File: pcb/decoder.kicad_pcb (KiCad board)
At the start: 2 copper layers, 50 x 30 mm, 76 parts, among them J1 Conn_01x03_Socket, J2 Conn_01x03_Socket, J3 Conn_01x02_Socket, J4 Conn_01x02_Socket, J5 Conn_01x02_Socket, J6 Conn_01x02_Socket, J7 Conn_01x02_Socket, J8 Conn_01x03_Socket, Q1 IRLZ44N, Q10 BC817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

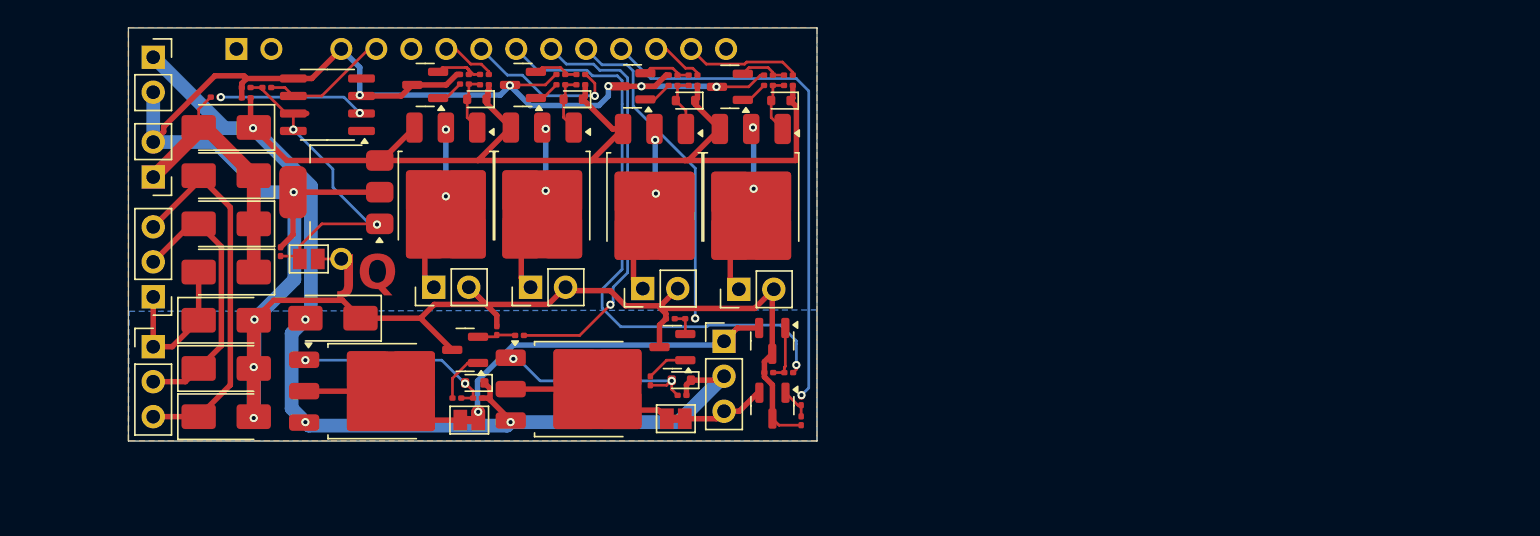
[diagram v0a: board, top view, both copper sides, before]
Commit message: make PCB smaller
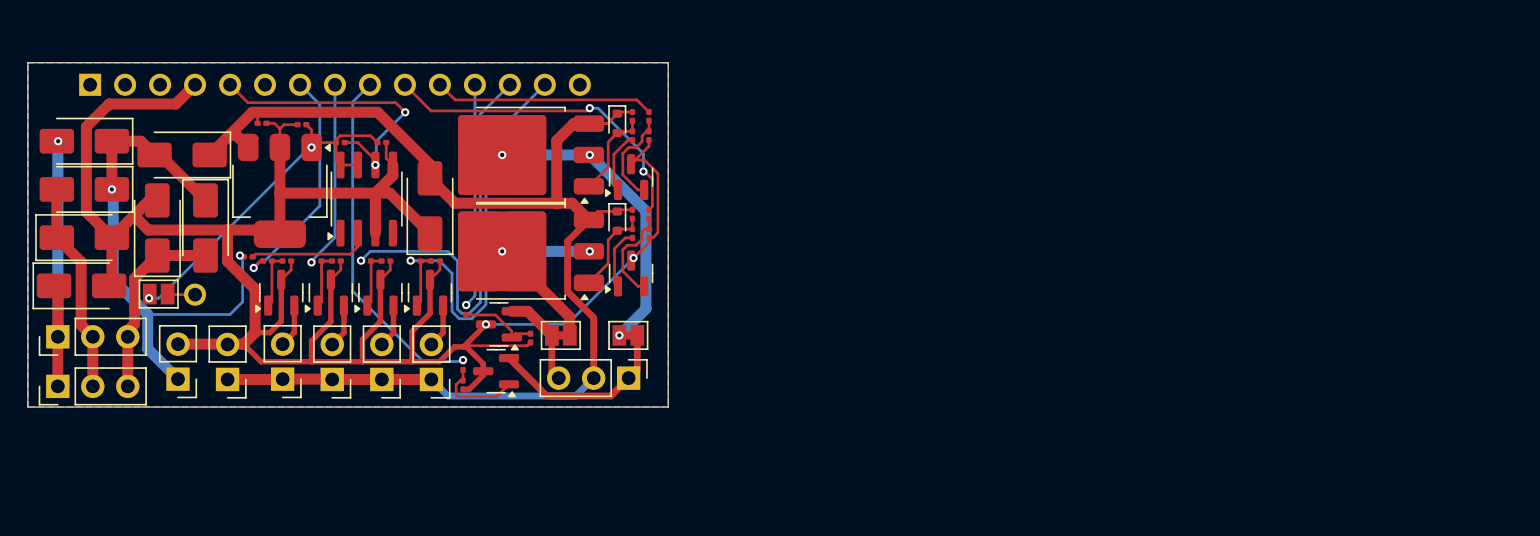
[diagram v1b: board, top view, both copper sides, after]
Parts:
- removed D10, D13, D14, D9: 15V, Diode_SMD:D_SOD-523
- removed J7: Conn_01x02_Socket, Connector_PinHeader_2.54mm:PinHeader_1x02_P2.54mm_Vertical
- removed Q11, Q13, Q9: FQP27P06, Package_TO_SOT_SMD:TO-252-3_TabPin2
- removed Q12, Q15: BC817, Package_TO_SOT_SMD:SOT-23
- removed R19, R28: 100, Capacitor_SMD:C_0201_0603Metric
- removed R20, R22, R26, R30: 2k, Capacitor_SMD:C_0201_0603Metric
- removed R21, R25, R27, R29: 100k, Capacitor_SMD:C_0201_0603Metric
- removed REF**: PinSocket_1x02_P2.54mm_Vertical, Connector_PinSocket_2.54mm:PinSocket_1x02_P2.54mm_Vertical
- added C1: 1mF, Connector_PinHeader_2.54mm:PinHeader_1x02_P2.54mm_Vertical, F.Cu at (39.1, 48.0)
- added J9: Conn_01x02_Socket, Connector_PinHeader_2.54mm:PinHeader_1x02_P2.54mm_Vertical, F.Cu at (50.3, 48.0)
- added Q14: FDN5630, Package_TO_SOT_SMD:SOT-23, F.Cu at (50.2, 41.7)
- added R31: 100k, Capacitor_SMD:C_0201_0603Metric, F.Cu at (50.6, 39.4)
- added R32: 100, Capacitor_SMD:C_0201_0603Metric, F.Cu at (49.2, 39.4)
- D11, D12: value 15V -> BZT52C15
- D8: value D_TVS -> SMBJ24CA
- Q1, Q4: value IRLZ44N -> FDN5630
- Q10, Q8: value BC817 -> FDN5630
- Q7: value FQP27P06 -> FDN5630; footprint Package_TO_SOT_SMD:TO-252-3_TabPin2 -> Package_TO_SOT_SMD:SOT-23
- R18: value 100k -> 100
- moved Q10 26.4 mm to (53.8, 41.7), turned to 90 degrees
- moved R18 26.1 mm to (42.0, 39.4), turned to 180 degrees
- moved R5 25.2 mm to (56.4, 43.0)
- moved R14 23.7 mm to (56.2, 47.0), turned to 90 degrees
- moved R4 23.3 mm to (68.5, 28.9), turned to -90 degrees
- moved R8 22.9 mm to (68.5, 30.3), turned to 90 degrees
- moved R23 22.6 mm to (54.2, 39.4), turned to 180 degrees
- moved R24 22.6 mm to (52.8, 39.4), turned to 180 degrees
- moved R6 22.2 mm to (56.2, 48.4), turned to 90 degrees
- moved D11 21.5 mm to (67.4, 29.4), turned to -90 degrees
- moved Q1 20.7 mm to (58.8, 44.0), turned to 180 degrees
- moved R2 20.5 mm to (61.1, 45.0)
- moved Q4 20.2 mm to (58.6, 47.4), turned to 180 degrees
- moved Q3 20.2 mm to (60.3, 31.7), turned to 180 degrees
- moved R17 18.7 mm to (43.4, 39.4)
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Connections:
- net 5V renamed /5V
- net AC1 renamed Net-(D15-A)
- net AC2 renamed Net-(D1-A)
- net AC3 renamed Net-(D2-A)
- net Motor_A renamed /Motor_A
- net Motor_A1 renamed /Motor_A1
- net Motor_B renamed /Motor_B
- net Motor_B1 renamed /Motor_B1
- net VCC renamed /VCC
- A1 pad 4: GND -> /GND
- C2 pad 2: GND -> /GND
- C4 pad 1: GND -> /GND
- C5 pad 1: GND -> /GND
- C5 pad 2: VM -> /VM
- D11 pad 1: VM -> /VM
- D12 pad 1: VM -> /VM
- D3 pad 2: GND -> /GND
- D4 pad 2: GND -> /GND
- D5 pad 2: GND -> /GND
- D6 pad 1: VM -> /VM
- D8 pad 1: GND -> /GND
- D8 pad 2: VM -> /VM
- J3 pad 2: GND -> /GND
- J4 pad 1: Lamp2 -> /VM
- J4 pad 2: GND -> Net-(J4-Pin_2)
- J5 pad 1: Lamp1 -> /VM
- J5 pad 2: GND -> Net-(J5-Pin_2)
- J6 pad 1: Lamp3 -> /VM
- J6 pad 2: GND -> Net-(J6-Pin_2)
- J8 pad 2: VM -> /VM
- Q1 pad 3: GND -> /GND
- Q10 pad 1: Net-(Q10-C) -> Net-(Q10-G)
- Q10 pad 2: Net-(Q10-B) -> Net-(J6-Pin_2)
- Q10 pad 3: GND -> /GND
- Q2 pad 3: VM -> /VM
- Q3 pad 3: VM -> /VM
- Q4 pad 3: GND -> /GND
- Q5 pad 3: GND -> /GND
- Q6 pad 3: GND -> /GND
- Q7 pad 1: Net-(D10-A) -> Net-(Q7-G)
- Q7 pad 2: Lamp2 -> Net-(J4-Pin_2)
- Q7 pad 3: VM -> /GND
- Q8 pad 1: Net-(Q8-C) -> Net-(Q8-G)
- Q8 pad 2: Net-(Q8-B) -> Net-(J5-Pin_2)
- Q8 pad 3: GND -> /GND
- R10 pad 2: GND -> /GND
- R11 pad 2: VM -> /VM
- R12 pad 1: Net-(A1-D7) -> Net-(A1-D8)
- R13 pad 2: GND -> /GND
- R15 pad 1: Net-(D9-A) -> /GND
- R15 pad 2: VM -> Net-(Q7-G)
- R16 pad 1: Net-(Q8-C) -> Net-(Q7-G)
- R16 pad 2: Net-(D9-A) -> Net-(A1-D5)
- R17 pad 1: Net-(Q8-B) -> /GND
- R17 pad 2: GND -> Net-(Q8-G)
- R18 pad 1: Net-(D10-A) -> Net-(Q8-G)
- R18 pad 2: VM -> Net-(A1-D4)
- R2 pad 1: GND -> /GND
- R23 pad 1: Net-(D13-A) -> /GND
- R23 pad 2: VM -> Net-(Q10-G)
- R24 pad 1: Net-(Q12-C) -> Net-(Q10-G)
- R24 pad 2: Net-(D13-A) -> Net-(A1-D11)
- R4 pad 1: VM -> /VM
- R6 pad 1: GND -> /GND
- R9 pad 1: Net-(A1-D8) -> Net-(A1-D7)
- U1 pad 2: GND -> /GND
- U1 pad 3: VM -> /VM
- U3 pad 3: GND -> /GND
- U3 pad 5: GND -> /GND
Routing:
- net GND: track 185.0 -> 0.00 mm, vias 9 -> 0
- net /GND: track 0.00 -> 166.1 mm, vias 0 -> 2
- net VM: track 148.4 -> 0.00 mm, vias 4 -> 0
- net /VM: track 0.00 -> 91.2 mm
- net Net-(A1-D10): track 3.88 -> 30.0 mm, vias 0 -> 1
- net Net-(A1-D9): track 37.2 -> 16.4 mm
- net /VCC: track 20.0 -> 38.9 mm, vias 0 -> 2
- net Net-(A1-D11): track 8.42 -> 27.1 mm, vias 0 -> 1
- net Net-(A1-D6): track 43.3 -> 25.8 mm
- net Net-(D15-A): track 27.8 -> 13.9 mm
- net Net-(A1-D4): track 3.97 -> 16.9 mm, vias 0 -> 1
- net /Motor_B1: track 9.90 -> 22.3 mm, vias 0 -> 3
- net Net-(A1-D2): track 9.30 -> 21.4 mm, vias 0 -> 2
- net /Motor_B: track 24.9 -> 13.7 mm, vias 1 -> 0
- net Net-(D2-A): track 11.2 -> 21.7 mm, vias 0 -> 1
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- added copper zone on B.Cu, net /GND
- added copper zone on F.Cu, net /VM
- removed copper zone on F.Cu, net GND
- removed copper zone on B.Cu, net VM
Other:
- board size 50 x 30 mm -> 46.5 x 25 mm
- board text removed: "JQ"

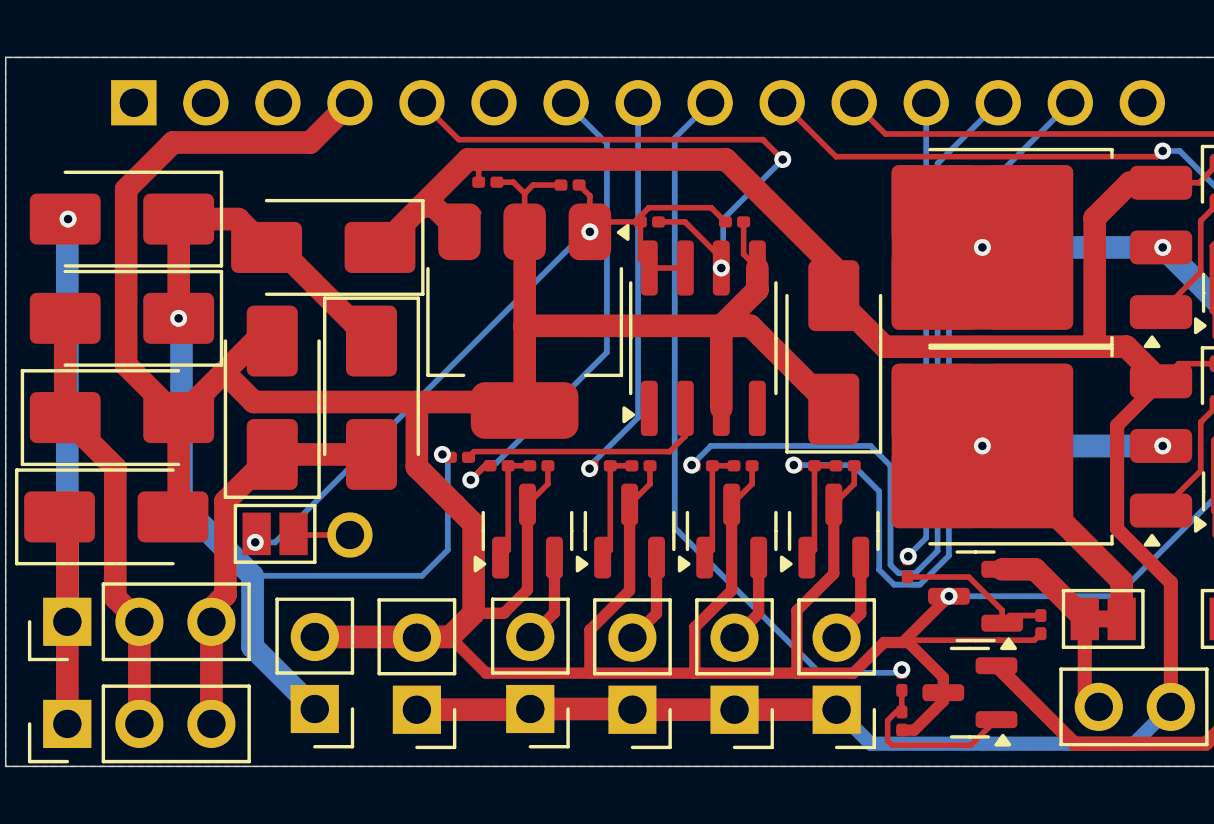
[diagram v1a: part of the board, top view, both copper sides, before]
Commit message: fix some pcb part numbers
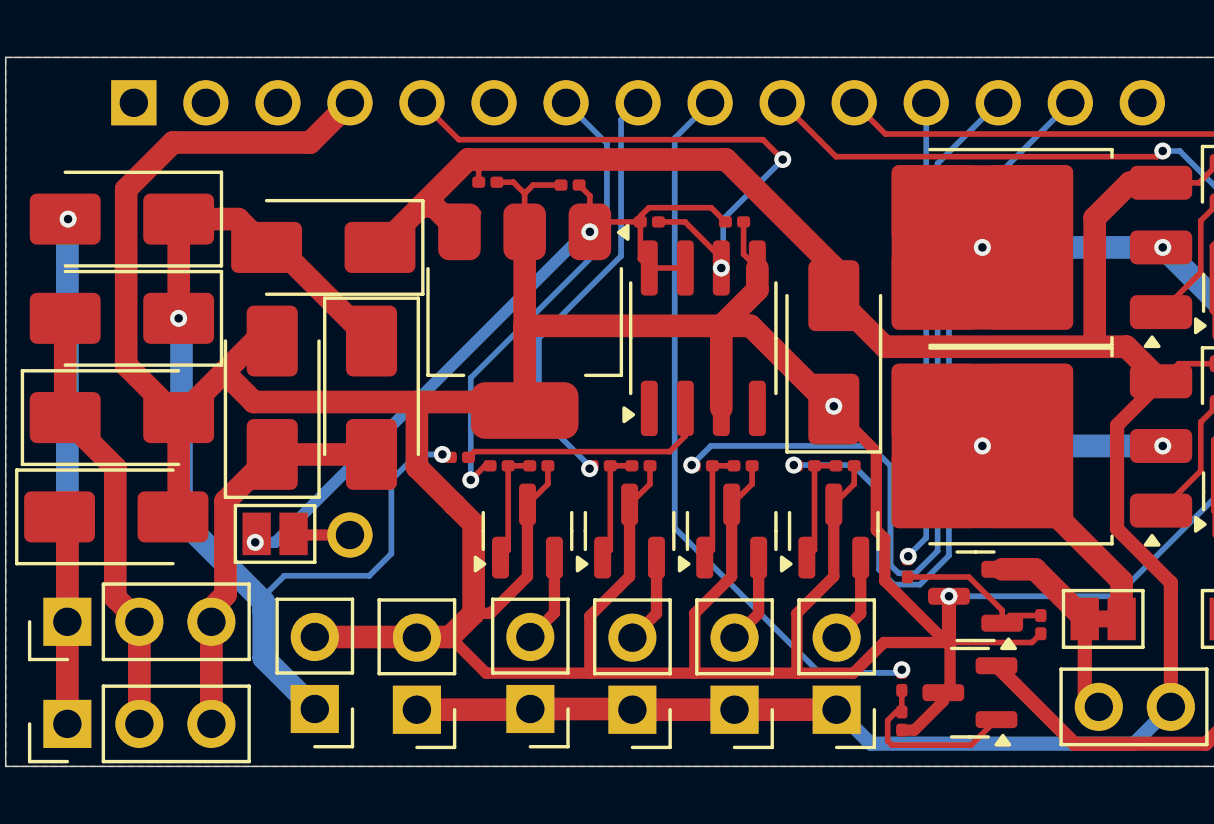
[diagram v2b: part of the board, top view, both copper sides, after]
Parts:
- D11, D12: value BZT52C15 -> BZT585B15T-7
- D8: value SMBJ24CA -> SMAJ24CA
- Q2, Q3: value FQP27P06 -> ROHM RD3L08BBJHRBTL
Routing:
- net /GND: track 166.1 -> 174.7 mm, vias 2 -> 3
- net Net-(A1-D5): track 13.7 -> 15.2 mm

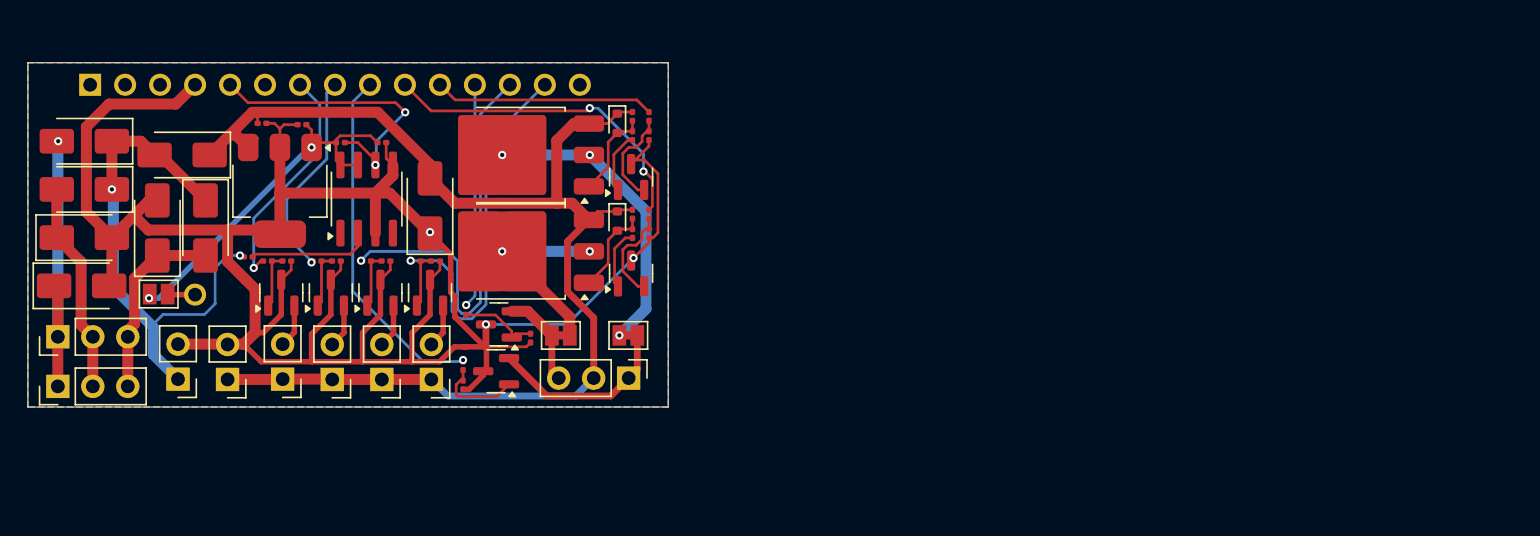
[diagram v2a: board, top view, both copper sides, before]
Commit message: add tests
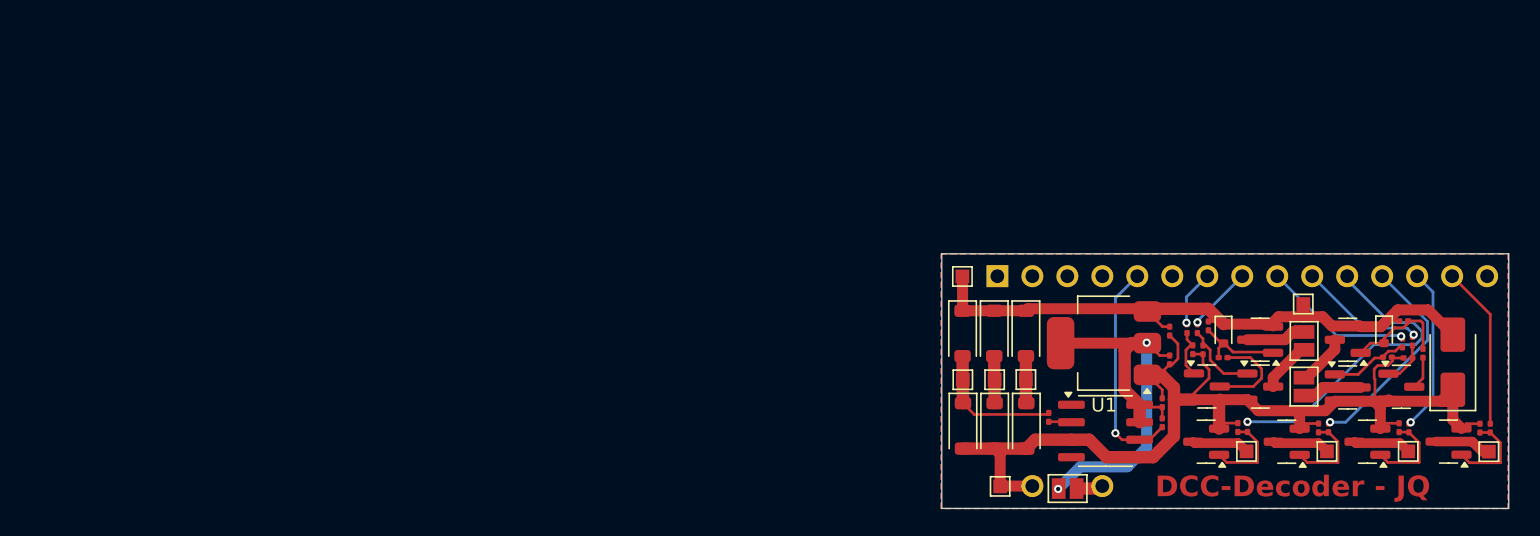
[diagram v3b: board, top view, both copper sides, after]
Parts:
- removed C1: 1mF, Connector_PinHeader_2.54mm:PinHeader_1x02_P2.54mm_Vertical
- removed D6: SS34, Diode_SMD:D_SMA
- removed J8: Conn_01x03_Socket, Connector_PinHeader_2.54mm:PinHeader_1x03_P2.54mm_Vertical
- removed JP3: Jumper_2_Bridged, Jumper:SolderJumper-2_P1.3mm_Bridged_Pad1.0x1.5mm
- added J11: Conn_01x01_Socket, TestPoint:TestPoint_Pad_1.0x1.0mm, F.Cu at (95.2, 55.8)
- added J12: Conn_01x01_Socket, TestPoint:TestPoint_Pad_1.0x1.0mm, F.Cu at (92.5, 40.5)
- added J7: Conn_01x01_Socket, TestPoint:TestPoint_Pad_1.0x1.0mm, F.Cu at (113.1, 53.2)
- added JP4: Jumper_2_Open, Jumper:SolderJumper-2_P1.3mm_Open_Pad1.0x1.5mm, F.Cu at (117.3, 48.5)
- D1, D15, D2, D3, D4, D5: value SS34 -> MBR120VLSFT1G; footprint Diode_SMD:D_SMA -> Diode_SMD:D_SOD-123
- J1, J2: value Conn_01x03_Socket -> Conn_01x01_Socket; footprint Connector_PinHeader_2.54mm:PinHeader_1x03_P2.54mm_Vertical -> TestPoint:TestPoint_Pad_1.0x1.0mm
- J3, J4, J5, J6, J9: value Conn_01x02_Socket -> Conn_01x01_Socket; footprint Connector_PinHeader_2.54mm:PinHeader_1x02_P2.54mm_Vertical -> TestPoint:TestPoint_Pad_1.0x1.0mm
- JP2: value Jumper_2_Bridged -> Jumper_2_Open; footprint Jumper:SolderJumper-2_P1.3mm_Bridged_Pad1.0x1.5mm -> Jumper:SolderJumper-2_P1.3mm_Open_Pad1.0x1.5mm
- Q2, Q3: value ROHM RD3L08BBJHRBTL -> NTR4171P; footprint Package_TO_SOT_SMD:TO-252-3_TabPin2 -> Package_TO_SOT_SMD:SOT-23
- U1: value LM7805 -> AMS1117
- moved J2 104.0 mm to (130.7, 53.2), turned to 180 degrees
- moved J1 98.4 mm to (124.8, 53.2), turned to 180 degrees
- moved R16 86.0 mm to (130.8, 51.5), turned to 90 degrees
- moved R15 83.9 mm to (130.0, 51.5), turned to -90 degrees
- moved R18 83.8 mm to (124.9, 51.5), turned to 90 degrees
- moved J3 83.6 mm to (118.9, 53.2)
- moved Q7 81.9 mm to (127.8, 52.5), turned to 180 degrees
- moved R17 81.7 mm to (124.2, 51.5), turned to -90 degrees
- moved Q8 79.6 mm to (121.9, 52.5), turned to 180 degrees
- moved D8 75.1 mm to (128.1, 46.7)
- moved D2 69.8 mm to (97.1, 44.7), turned to -90 degrees
- moved D5 69.3 mm to (97.1, 51.4), turned to -90 degrees
- moved R5 68.1 mm to (124.4, 45.4)
- moved C5 67.6 mm to (107.5, 44.5), turned to 90 degrees
- moved D4 67.5 mm to (94.8, 51.4), turned to -90 degrees
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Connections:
- A1 pad 4: /GND -> unconnected-(A1-GND-Pad4)
- D1 pad 1: /VCC -> /VM
- D15 pad 1: /VCC -> /VM
- D2 pad 1: /VCC -> /VM
- J1 pad 1: Net-(D2-A) -> Net-(J1-Pin_1)
- J2 pad 1: Net-(D2-A) -> Net-(J2-Pin_1)
- J3 pad 1: /VCC -> Net-(J3-Pin_1)
- J4 pad 1: /VM -> Net-(D2-A)
- J5 pad 1: /VM -> Net-(D1-A)
- J6 pad 1: /VM -> Net-(D15-A)
- JP2 pad 1: /Motor_A -> /Motor_B1
- JP2 pad 2: /Motor_A1 -> /Motor_B
- Q1 pad 2: /Motor_A -> /GND
- Q1 pad 3: /GND -> /Motor_A
- Q10 pad 2: Net-(J6-Pin_2) -> /GND
- Q10 pad 3: /GND -> Net-(J3-Pin_1)
- Q14 pad 2: Net-(J9-Pin_2) -> /GND
- Q14 pad 3: /GND -> Net-(J7-Pin_1)
- Q2 pad 2: /Motor_A1 -> /VM
- Q2 pad 3: /VM -> /Motor_A1
- Q3 pad 2: /Motor_B1 -> /VM
- Q3 pad 3: /VM -> /Motor_B1
- Q4 pad 2: /Motor_B -> /GND
- Q4 pad 3: /GND -> /Motor_B
- Q5 pad 1: Net-(Q5-C) -> Net-(Q5-B)
- Q5 pad 2: Net-(Q5-B) -> /GND
- Q5 pad 3: /GND -> Net-(Q5-C)
- Q6 pad 1: Net-(Q6-C) -> Net-(Q6-B)
- Q6 pad 2: Net-(Q6-B) -> /GND
- Q6 pad 3: /GND -> Net-(Q6-C)
- Q7 pad 2: Net-(J4-Pin_2) -> /GND
- Q7 pad 3: /GND -> Net-(J2-Pin_1)
- Q8 pad 2: Net-(J5-Pin_2) -> /GND
- Q8 pad 3: /GND -> Net-(J1-Pin_1)
- R1 pad 2: /VCC -> Net-(D15-A)
- R12 pad 1: Net-(A1-D8) -> Net-(A1-D4)
- R14 pad 2: Net-(A1-D6) -> Net-(A1-D5)
- R16 pad 2: Net-(A1-D5) -> Net-(A1-D11)
- R18 pad 2: Net-(A1-D4) -> Net-(A1-D10)
- R24 pad 2: Net-(A1-D11) -> Net-(A1-D9)
- R32 pad 2: Net-(A1-D10) -> Net-(A1-D8)
- R5 pad 2: Net-(A1-D9) -> Net-(A1-D6)
- U1 pad 1: /5V -> /GND
- U1 pad 2: /GND -> /5V
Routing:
- net /GND: track 174.7 -> 81.8 mm, vias 3 -> 0
- net /VM: track 91.2 -> 46.2 mm
- net /VCC: track 38.6 -> 0.00 mm, vias 2 -> 0
- net Net-(D2-A): track 21.7 -> 3.42 mm, vias 1 -> 0
- net Net-(A1-D10): track 30.0 -> 11.9 mm
- net /Motor_B1: track 22.3 -> 4.36 mm, vias 3 -> 0
- net Net-(A1-D11): track 27.1 -> 11.9 mm, vias 1 -> 0
- net Net-(A1-D7): track 24.1 -> 9.32 mm, vias 2 -> 1
- net Net-(A1-D6): track 25.8 -> 11.2 mm
- net Net-(A1-D4): track 16.8 -> 4.13 mm
- net Net-(D1-A): track 15.4 -> 3.42 mm
- net Net-(A1-D5): track 15.2 -> 4.84 mm
- net /Motor_B: track 13.7 -> 3.74 mm
- net /Motor_A1: track 12.3 -> 3.80 mm, vias 2 -> 0
- net Net-(U3-A): track 8.93 -> 1.66 mm
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- added copper zone on F.Cu, net /GND
- removed copper zone on F.Cu, net /VM
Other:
- board size 46.5 x 25 mm -> 41.2 x 18.5 mm
- board text added: "DCC-Decoder - JQ"
